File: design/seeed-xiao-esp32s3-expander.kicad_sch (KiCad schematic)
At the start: 15 parts, among them J1 Header 1x7 2.54mm, J2 Header 1x7 2.54mm, J3 30pin, K1 TS-1185E, U1 Wio-SX1262

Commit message: Initial schematic for breakout
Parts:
- removed C1: 100nF, Capacitor:C0402, symbol libdb:Capacitors/302010004
- removed J2: Header 1x7 2.54mm, Connector:H7-2.54, symbol libdb:Connector/320020216
- removed R1: 10K, Resistor:R0402, symbol libdb:Resistors/301010004
- removed R4, R5, R6, R7: 47R, Resistor:R0402, symbol libdb:Resistors/301010878
- removed TP1: Test Point, Misc:TP-D3_5c2_2mm, symbol Seeed_libdb:Misc/TP-D3_5c2_2mm
- removed U1: Wio-SX1262, Module:MODULE12P-1.27-11X11.6MM, symbol libdb:Module/114993390
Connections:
- net GPIO14: now also J1.1
- net GPIO15: now also J1.2
- net GPIO16: now also J1.3
- net GPIO17: now also J1.4
- net GPIO18: now also J1.5
- net GPIO47: now also J1.6
- net GPIO48: now also J1.7
- net LORA_BUSY: no longer names the net of J3.11
- net LORA_BUSY: no longer J1.2
- net LORA_DIO1: no longer names the net of J3.13
- net LORA_DIO1: no longer J1.1
- net LORA_RF_SW1: no longer names the net of J3.15
- net LORA_RF_SW1: no longer J1.5
- net LORA_RST: no longer names the net of J3.7
- net LORA_RST: no longer J1.3
- net LORA_SPI_MISO: no longer names the net of J3.8
- net LORA_SPI_MOSI: no longer names the net of J3.10
- net LORA_SPI_NSS: no longer names the net of J3.9
- net LORA_SPI_NSS: no longer J1.4
- net LORA_SPI_SCK: no longer names the net of J3.6
- no-connect marks 11 -> 14
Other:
- moved on the sheet: J1

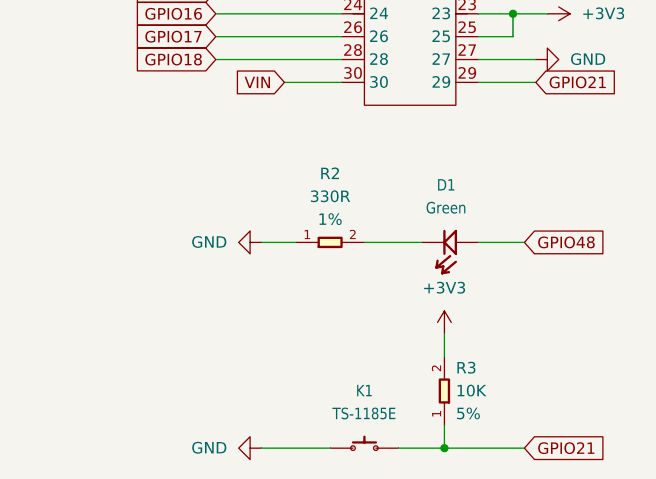
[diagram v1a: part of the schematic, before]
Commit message: Remove LED and button
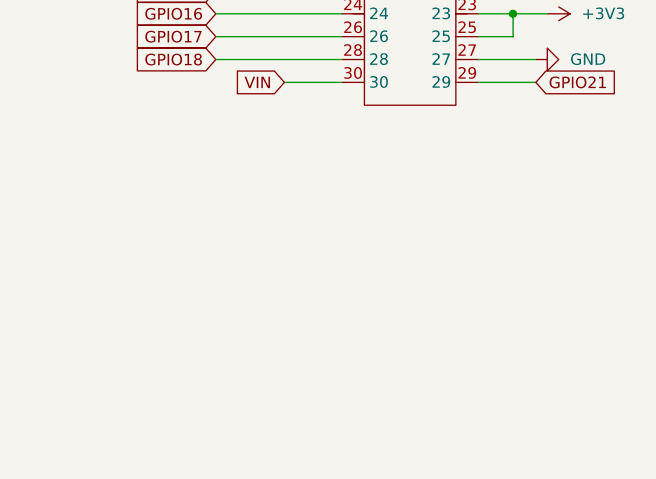
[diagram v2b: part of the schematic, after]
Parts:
- removed D1: Green, Diode:LED-0603, symbol libdb:Diode/304090043
- removed K1: TS-1185E, Switch:BUTTON2P_3_9X3X2MM, symbol libdb:Switch/311020068
- removed R2: 330R, Resistor:R0402, symbol libdb:Resistors/301010466
- removed R3: 10K, Resistor:R0402, symbol libdb:Resistors/301010004

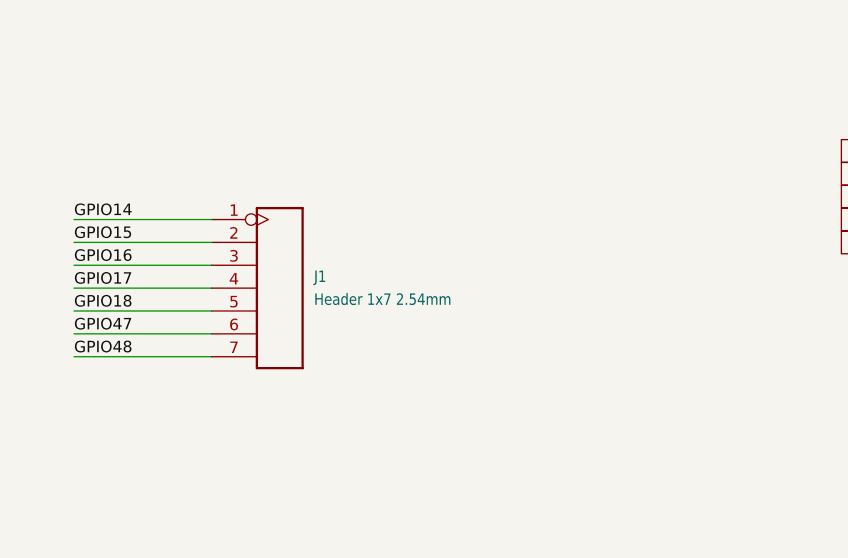
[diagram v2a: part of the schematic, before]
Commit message: Add more organized header pad combo
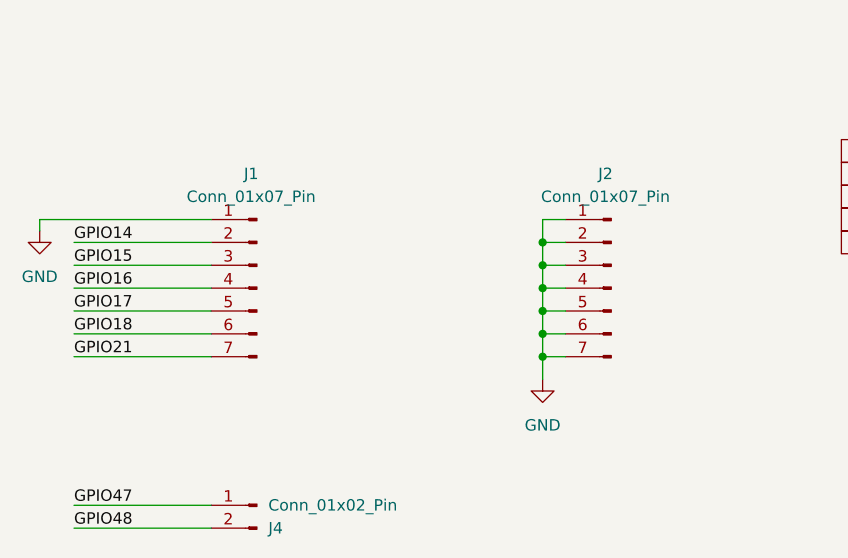
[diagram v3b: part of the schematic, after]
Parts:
- removed J1: Header 1x7 2.54mm, Connector:H7-2.54, symbol libdb:Connector/320020216
- added J1, J2: Conn_01x07_Pin, seeed-xiao-esp32s3-expander:PinHeader_1x07_P2.54mm, symbol Connector:Conn_01x07_Pin
- added J4: Conn_01x02_Pin, symbol Connector:Conn_01x02_Pin
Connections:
- net GND: now also J1.1 (Pin_1), J2.1 (Pin_1), J2.2 (Pin_2), J2.3 (Pin_3), J2.4 (Pin_4), J2.5 (Pin_5), J2.6 (Pin_6), J2.7 (Pin_7)
- net GPIO14: now also J1.2 (Pin_2)
- net GPIO15: now also J1.3 (Pin_3)
- net GPIO16: now also J1.4 (Pin_4)
- net GPIO17: now also J1.5 (Pin_5)
- net GPIO18: now also J1.6 (Pin_6)
- net GPIO21: now also J1.7 (Pin_7)
- net GPIO47: now also J4.1 (Pin_1)
- net GPIO48: now also J4.2 (Pin_2)

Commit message: Add remaining gpio and pads
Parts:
- removed J1, J2: Conn_01x07_Pin, seeed-xiao-esp32s3-expander:PinHeader_1x07_P2.54mm, symbol Connector:Conn_01x07_Pin
- removed J4: Conn_01x02_Pin, symbol Connector:Conn_01x02_Pin
- added J1, J2: Conn_01x07, seeed-xiao-esp32s3-expander:PinHeader_1x07_P2.54mm, symbol Connector_Generic:Conn_01x07
- added J4: Conn_01x02, Connector_PinHeader_2.54mm:PinHeader_1x02_P2.54mm_Vertical, symbol Connector_Generic:Conn_01x02
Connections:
- net GND: now also J1.1 (Pin_1), J2.1 (Pin_1), J2.2 (Pin_2), J2.3 (Pin_3), J2.4 (Pin_4), J2.5 (Pin_5), J2.6 (Pin_6), J2.7 (Pin_7)
- net GPIO14: now also J1.2 (Pin_2)
- net GPIO15: now also J1.3 (Pin_3)
- net GPIO16: now also J1.4 (Pin_4)
- net GPIO17: now also J1.5 (Pin_5)
- net GPIO18: now also J1.6 (Pin_6)
- net GPIO21: now also J1.7 (Pin_7)
- net GPIO47: now also J4.1 (Pin_1)
- net GPIO48: now also J4.2 (Pin_2)
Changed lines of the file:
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@@
 	)
 	(symbol
-		(lib_id "Connector:Conn_01x02_Pin")
-		(at 91.44 114.3 0)
-		(mirror y)
+		(lib_id "Connector_Generic:Conn_01x07")
+		(at 130.81 90.17 0)
 		(unit 1)
 		(body_style 1)
@@
 		(in_pos_files yes)
 		(dnp no)
-		(property "Reference" "J4"
-			(at 92.71 116.8401 0)
-			(show_name no)
-			(do_not_autoplace no)
-			(effects
-				(font
-					(size 1.27 1.27)
-				)
-				(justify right)
-			)
-		)
-		(property "Value" "Conn_01x02_Pin"
-			(at 92.71 114.3001 0)
-			(show_name no)
-			(do_not_autoplace no)
-			(effects
-				(font
-					(size 1.27 1.27)
-				)
-				(justify right)
-			)
-		)
-		(property "Footprint" ""
-			(at 91.44 114.3 0)
+		(fields_autoplaced yes)
+		(property "Reference" "J2"
+			(at 133.35 88.8999 0)
+			(show_name no)
+			(do_not_autoplace no)
+			(effects
+				(font
+					(size 1.27 1.27)
+				)
+				(justify left)
+			)
+		)
+		(property "Value" "Conn_01x07"
+			(at 133.35 91.4399 0)
+			(show_name no)
+			(do_not_autoplace no)
+			(effects
+				(font
+					(size 1.27 1.27)
+				)
+				(justify left)
+			)
+		)
+		(property "Footprint" "seeed-xiao-esp32s3-expander:PinHeader_1x07_P2.54mm"
+			(at 130.81 90.17 0)
 			(hide yes)
 			(show_name no)
@@
 		)
 		(property "Datasheet" ""
-			(at 91.44 114.3 0)
-			(hide yes)
-			(show_name no)
-			(do_not_autoplace no)
-			(effects
-				(font
-					(size 1.27 1.27)
-				)
-			)
-		)
-		(property "Description" "Generic connector, single row, 01x02, script generated"
-			(at 91.44 114.3 0)
-			(hide yes)
-			(show_name no)
-			(do_not_autoplace no)
-			(effects
-				(font
-					(size 1.27 1.27)
-				)
-			)
+			(at 130.81 90.17 0)
+			(hide yes)
+			(show_name no)
+			(do_not_autoplace no)
+			(effects
+				(font
+					(size 1.27 1.27)
+				)
+			)
+		)
+		(property "Description" "Generic connector, single row, 01x07, script generated (kicad-library-utils/schlib/autogen/connector/)"
+			(at 130.81 90.17 0)
+			(hide yes)
+			(show_name no)
+			(do_not_autoplace no)
+			(effects
+				(font
+					(size 1.27 1.27)
+				)
+			)
+		)
+		(pin "3"
+		)
+		(pin "1"
+		)
+		(pin "4"
+		)
+		(pin "5"
 		)
 		(pin "2"
 		)
-		(pin "1"
+		(pin "7"
+		)
+		(pin "6"
 		)
 		(instances
 			(project "seeed-xiao-esp32s3-expander"
 				(path "/ddd1596a-1fdb-4457-bd34-9991d769f287"
-					(reference "J4")
+					(reference "J2")
+					(unit 1)
+				)
+			)
+		)
+	)
+	(symbol
+		(lib_id "Connector_Generic:Conn_01x07")
+		(at 91.44 90.17 0)
+		(unit 1)
+		(body_style 1)
+		(exclude_from_sim no)
+		(in_bom yes)
+		(on_board yes)
+		(in_pos_files yes)
+		(dnp no)
+		(fields_autoplaced yes)
+		(property "Reference" "J1"
+			(at 93.98 88.8999 0)
+			(show_name no)
+			(do_not_autoplace no)
+			(effects
+				(font
+					(size 1.27 1.27)
+				)
+				(justify left)
+			)
+		)
+		(property "Value" "Conn_01x07"
+			(at 93.98 91.4399 0)
+			(show_name no)
+			(do_not_autoplace no)
+			(effects
+				(font
+					(size 1.27 1.27)
+				)
+				(justify left)
+			)
+		)
+		(property "Footprint" "seeed-xiao-esp32s3-expander:PinHeader_1x07_P2.54mm"
+			(at 91.44 90.17 0)
+			(hide yes)
+			(show_name no)
+			(do_not_autoplace no)
+			(effects
+				(font
+					(size 1.27 1.27)
+				)
+			)
+		)
+		(property "Datasheet" ""
+			(at 91.44 90.17 0)
+			(hide yes)
+			(show_name no)
+			(do_not_autoplace no)
+			(effects
+				(font
+					(size 1.27 1.27)
+				)
+			)
+		)
+		(property "Description" "Generic connector, single row, 01x07, script generated (kicad-library-utils/schlib/autogen/connector/)"
+			(at 91.44 90.17 0)
+			(hide yes)
+			(show_name no)
+			(do_not_autoplace no)
+			(effects
+				(font
+					(size 1.27 1.27)
+				)
+			)
+		)
+		(pin "3"
+		)
+		(pin "1"
+		)
+		(pin "4"
+		)
+		(pin "5"
+		)
+		(pin "2"
+		)
+		(pin "7"
+		)
+		(pin "6"
+		)
+		(instances
+			(project "seeed-xiao-esp32s3-expander"
+				(path "/ddd1596a-1fdb-4457-bd34-9991d769f287"
+					(reference "J1")
 					(unit 1)
 				)
@@
 	)
 	(symbol
-		(lib_id "Connector:Conn_01x07_Pin")
-		(at 130.81 90.17 0)
-		(mirror y)
+		(lib_id "Connector_Generic:Conn_01x02")
+		(at 91.44 114.3 0)
 		(unit 1)
 		(body_style 1)
@@
 		(in_pos_files yes)
 		(dnp no)
-		(property "Reference" "J2"
-			(at 130.175 77.47 0)
-			(show_name no)
-			(do_not_autoplace no)
-			(effects
-				(font
-					(size 1.27 1.27)
-				)
-			)
-		)
-		(property "Value" "Conn_01x07_Pin"
-			(at 130.175 80.01 0)
-			(show_name no)
-			(do_not_autoplace no)
-			(effects
-				(font
-					(size 1.27 1.27)
-				)
-			)
-		)
-		(property "Footprint" "seeed-xiao-esp32s3-expander:PinHeader_1x07_P2.54mm"
-			(at 130.81 90.17 0)
+		(fields_autoplaced yes)
+		(property "Reference" "J4"
+			(at 93.98 114.2999 0)
+			(show_name no)
+			(do_not_autoplace no)
+			(effects
+				(font
+					(size 1.27 1.27)
+				)
+				(justify left)
+			)
+		)
+		(property "Value" "Conn_01x02"
+			(at 93.98 116.8399 0)
+			(show_name no)
+			(do_not_autoplace no)
+			(effects
+				(font
+					(size 1.27 1.27)
+				)
+				(justify left)
+			)
+		)
+		(property "Footprint" "Connector_PinHeader_2.54mm:PinHeader_1x02_P2.54mm_Vertical"
+			(at 91.44 114.3 0)
 			(hide yes)
 			(show_name no)
@@
 		)
 		(property "Datasheet" ""
-			(at 130.81 90.17 0)
-			(hide yes)
-			(show_name no)
-			(do_not_autoplace no)
-			(effects
-				(font
-					(size 1.27 1.27)
-				)
-			)
-		)
-		(property "Description" "Generic connector, single row, 01x07, script generated"
-			(at 130.81 90.17 0)
-			(hide yes)
-			(show_name no)
-			(do_not_autoplace no)
-			(effects
-				(font
-					(size 1.27 1.27)
-				)
-			)
-		)
-		(pin "3"
-		)
-		(pin "4"
-		)
-		(pin "5"
+			(at 91.44 114.3 0)
+			(hide yes)
+			(show_name no)
+			(do_not_autoplace no)
+			(effects
+				(font
+					(size 1.27 1.27)
+				)
+			)
+		)
+		(property "Description" "Generic connector, single row, 01x02, script generated (kicad-library-utils/schlib/autogen/connector/)"
+			(at 91.44 114.3 0)
+			(hide yes)
+			(show_name no)
+			(do_not_autoplace no)
+			(effects
+				(font
+					(size 1.27 1.27)
+				)
+			)
 		)
 		(pin "1"
 		)
-		(pin "6"
-		)
 		(pin "2"
-		)
-		(pin "7"
 		)
 		(instances
 			(project "seeed-xiao-esp32s3-expander"
 				(path "/ddd1596a-1fdb-4457-bd34-9991d769f287"
-					(reference "J2")
+					(reference "J4")
 					(unit 1)
 				)
-			)
-		)
-	)
-	(symbol
-		(lib_id "Connector:Conn_01x07_Pin")
-		(at 91.44 90.17 0)
-		(mirror y)
-		(unit 1)
-		(body_style 1)
-		(exclude_from_sim no)
-		(in_bom yes)
-		(on_board yes)
-		(in_pos_files yes)
-		(dnp no)
-		(property "Reference" "J1"
-			(at 90.805 77.47 0)
-			(show_name no)
-			(do_not_autoplace no)
-			(effects
-				(font
-					(size 1.27 1.27)
-				)
-			)
-		)
-		(property "Value" "Conn_01x07_Pin"
-			(at 90.805 80.01 0)
-			(show_name no)
-			(do_not_autoplace no)
-			(effects
-				(font
-					(size 1.27 1.27)
-				)
-			)
-		)
-		(property "Footprint" "seeed-xiao-esp32s3-expander:PinHeader_1x07_P2.54mm"
-			(at 91.44 90.17 0)
-			(hide yes)
-			(show_name no)
-			(do_not_autoplace no)
-			(effects
-				(font
-					(size 1.27 1.27)
-				)
-			)
-		)
-		(property "Datasheet" ""
-			(at 91.44 90.17 0)
-			(hide yes)
-			(show_name no)
-			(do_not_autoplace no)
-			(effects
-				(font
-					(size 1.27 1.27)
-				)
-			)
-		)
-		(property "Description" "Generic connector, single row, 01x07, script generated"
-			(at 91.44 90.17 0)
-			(hide yes)
-			(show_name no)
-			(do_not_autoplace no)
-			(effects
-				(font
-					(size 1.27 1.27)
-				)
-			)
-		)
-		(pin "3"
-		)
-		(pin "4"
-		)
-		(pin "5"
-		)
-		(pin "1"
-		)
-		(pin "6"
-		)
-		(pin "2"
-		)
-		(pin "7"
-		)
-		(instances
-			(project "seeed-xiao-esp32s3-expander"
-				(path "/ddd1596a-1fdb-4457-bd34-9991d769f287"
-					(reference "J1")
-					(unit 1)
-				)

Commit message: Add VIN pin
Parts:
- added J5: Conn_01x01, Connector_PinHeader_2.54mm:PinHeader_1x01_P2.54mm_Vertical, symbol Connector_Generic:Conn_01x01
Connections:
- net VIN: now also J5.1 (Pin_1)
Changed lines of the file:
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@@
+	(wire
+		(pts
+			(xy 115.57 114.3) (xy 125.73 114.3)
+		)
+		(stroke
+			(width 0)
+			(type default)
+		)
+	)
 	(wire
 		(pts
@@
 	(label "GPIO17"
 		(at 71.12 92.71 0)
+		(effects
+			(font
+				(size 1.27 1.27)
+			)
+			(justify left bottom)
+		)
+	)
+	(label "VIN"
+		(at 115.57 114.3 0)
 		(effects
 			(font
@@
 					(unit 1)
 				)
+			)
+		)
+	)
+	(symbol
+		(lib_id "Connector_Generic:Conn_01x01")
+		(at 130.81 114.3 0)
+		(unit 1)
+		(body_style 1)
+		(exclude_from_sim no)
+		(in_bom yes)
+		(on_board yes)
+		(in_pos_files yes)
+		(dnp no)
+		(fields_autoplaced yes)
+		(property "Reference" "J5"
+			(at 133.35 113.0299 0)
+			(show_name no)
+			(do_not_autoplace no)
+			(effects
+				(font
+					(size 1.27 1.27)
+				)
+				(justify left)
+			)
+		)
+		(property "Value" "Conn_01x01"
+			(at 133.35 115.5699 0)
+			(show_name no)
+			(do_not_autoplace no)
+			(effects
+				(font
+					(size 1.27 1.27)
+				)
+				(justify left)
+			)
+		)
+		(property "Footprint" "Connector_PinHeader_2.54mm:PinHeader_1x01_P2.54mm_Vertical"
+			(at 130.81 114.3 0)
+			(hide yes)
+			(show_name no)
+			(do_not_autoplace no)
+			(effects
+				(font
+					(size 1.27 1.27)
+				)
+			)
+		)
+		(property "Datasheet" ""
+			(at 130.81 114.3 0)
+			(hide yes)
+			(show_name no)
+			(do_not_autoplace no)
+			(effects
+				(font
+					(size 1.27 1.27)
+				)
+			)
+		)
+		(property "Description" "Generic connector, single row, 01x01, script generated (kicad-library-utils/schlib/autogen/connector/)"
+			(at 130.81 114.3 0)
+			(hide yes)
+			(show_name no)
+			(do_not_autoplace no)
+			(effects
+				(font
+					(size 1.27 1.27)
+				)
+			)
+		)
+		(pin "1"
+		)
+		(instances
+			(project "seeed-xiao-esp32s3-expander"
+				(path "/ddd1596a-1fdb-4457-bd34-9991d769f287"
+					(reference "J5")
+					(unit 1)
+				)

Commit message: Replace GPIO21 breakout with 3V3
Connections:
- net +3V3: now also J1.7 (Pin_7)
- net GPIO21: no longer J1.7 (Pin_7)
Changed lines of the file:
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@@
-	(wire
-		(pts
-			(xy 71.12 97.79) (xy 86.36 97.79)
-		)
-		(stroke
-			(width 0)
-			(type default)
-		)
-	)
 	(wire
 		(pts
@@
 	(wire
 		(pts
+			(xy 67.31 97.79) (xy 67.31 96.52)
+		)
+		(stroke
+			(width 0)
+			(type default)
+		)
+	)
+	(wire
+		(pts
 			(xy 71.12 116.84) (xy 86.36 116.84)
 		)
@@
 		(pts
 			(xy 194.31 82.55) (xy 198.12 82.55)
+		)
+		(stroke
+			(width 0)
+			(type default)
+		)
+	)
+	(wire
+		(pts
+			(xy 67.31 97.79) (xy 86.36 97.79)
 		)
 		(stroke
@@
 	(label "GPIO48"
 		(at 71.12 116.84 0)
-		(effects
-			(font
-				(size 1.27 1.27)
-			)
-			(justify left bottom)
-		)
-	)
-	(label "GPIO21"
-		(at 71.12 97.79 0)
 		(effects
 			(font
@@
 		(in_pos_files yes)
 		(dnp no)
-		(fields_autoplaced yes)
 		(property "Reference" "#PWR015"
 			(at 67.31 90.17 0)
@@
 		)
 		(property "Value" "GND"
-			(at 67.31 88.9 0)
+			(at 64.516 87.376 0)
 			(show_name no)
 			(do_not_autoplace no)
@@
 					(unit 1)
 				)
+			)
+		)
+	)
+	(symbol
+		(lib_id "Power_Gnd:+3V3")
+		(at 67.31 96.52 0)
+		(unit 1)
+		(body_style 1)
+		(exclude_from_sim no)
+		(in_bom yes)
+		(on_board yes)
+		(in_pos_files yes)
+		(dnp no)
+		(property "Reference" "#PWR016"
+			(at 67.31 100.33 0)
+			(hide yes)
+			(show_name no)
+			(do_not_autoplace no)
+			(effects
+				(font
+					(size 1.27 1.27)
+				)
+			)
+		)
+		(property "Value" "+3V3"
+			(at 64.008 93.218 0)
+			(show_name no)
+			(do_not_autoplace no)
+			(effects
+				(font
+					(size 1.27 1.27)
+				)
+			)
+		)
+		(property "Footprint" ""
+			(at 67.31 96.52 0)
+			(hide yes)
+			(show_name no)
+			(do_not_autoplace no)
+			(effects
+				(font
+					(size 1.27 1.27)
+				)
+			)
+		)
+		(property "Datasheet" ""
+			(at 67.31 96.52 0)
+			(hide yes)
+			(show_name no)
+			(do_not_autoplace no)
+			(effects
+				(font
+					(size 1.27 1.27)
+				)
+			)
+		)
+		(property "Description" "Power symbol creates a global label with name \"+3V3\""
+			(at 67.31 96.52 0)
+			(hide yes)
+			(show_name no)
+			(do_not_autoplace no)
+			(effects
+				(font
+					(size 1.27 1.27)
+				)
+			)
+		)
+		(pin "1"
+		)
+		(instances
+			(project "seeed-xiao-esp32s3-expander"
+				(path "/ddd1596a-1fdb-4457-bd34-9991d769f287"
+					(reference "#PWR016")
+					(unit 1)
+				)
